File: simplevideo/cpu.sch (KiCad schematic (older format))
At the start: 8 parts, among them J2 Conn_01x08, J3 Conn_01x08, J4 Conn_01x08, J5 Conn_01x03, U18 WD65C02_, U19 74LS00, U27 28C256, U32 74LS138

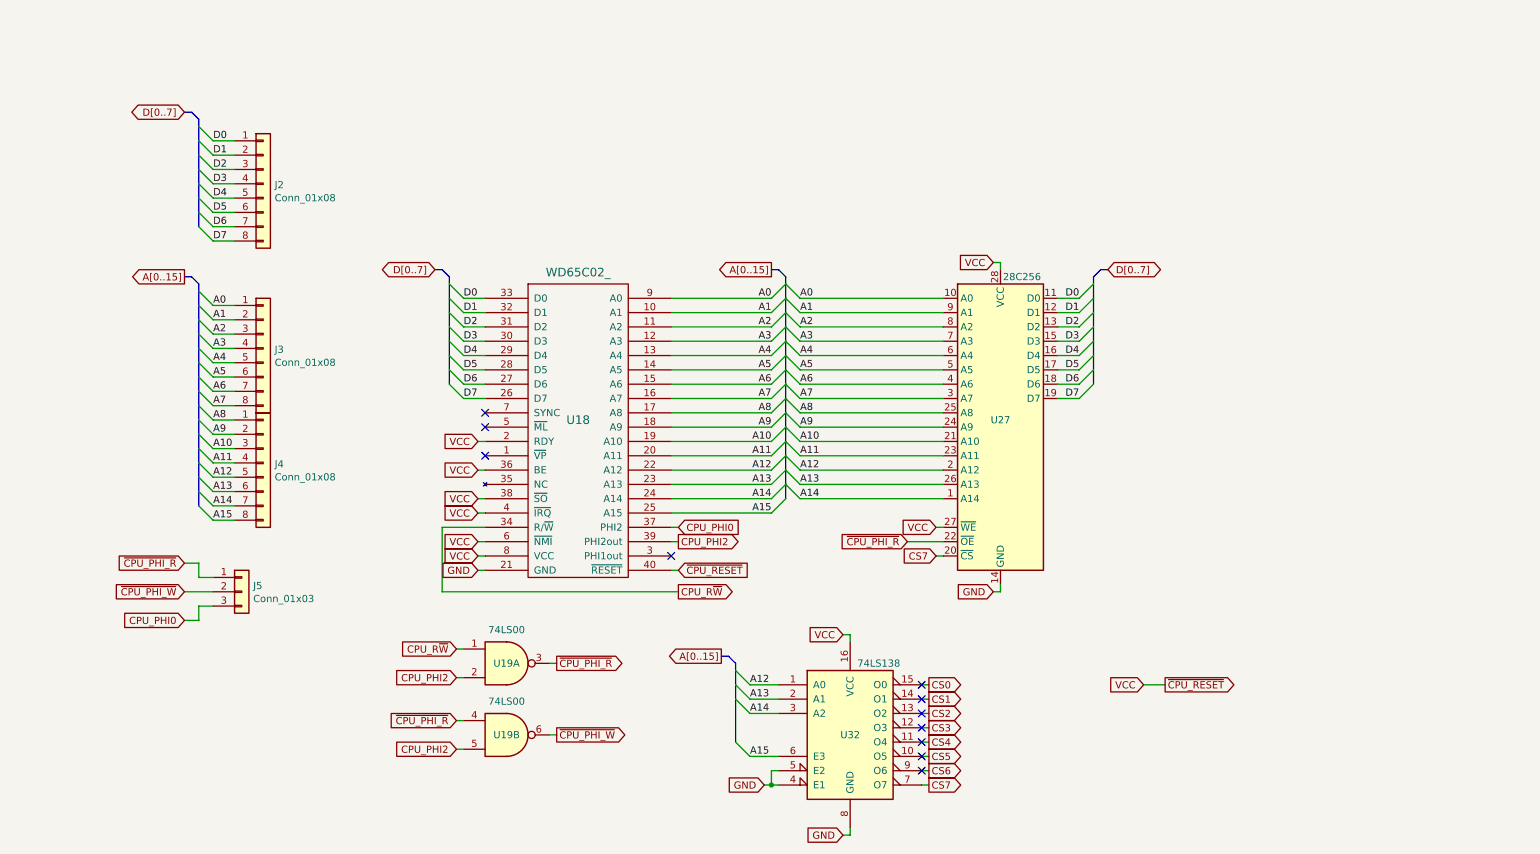
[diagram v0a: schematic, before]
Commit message: New address decoding scheme and complete breadboard layout, should be ready to build
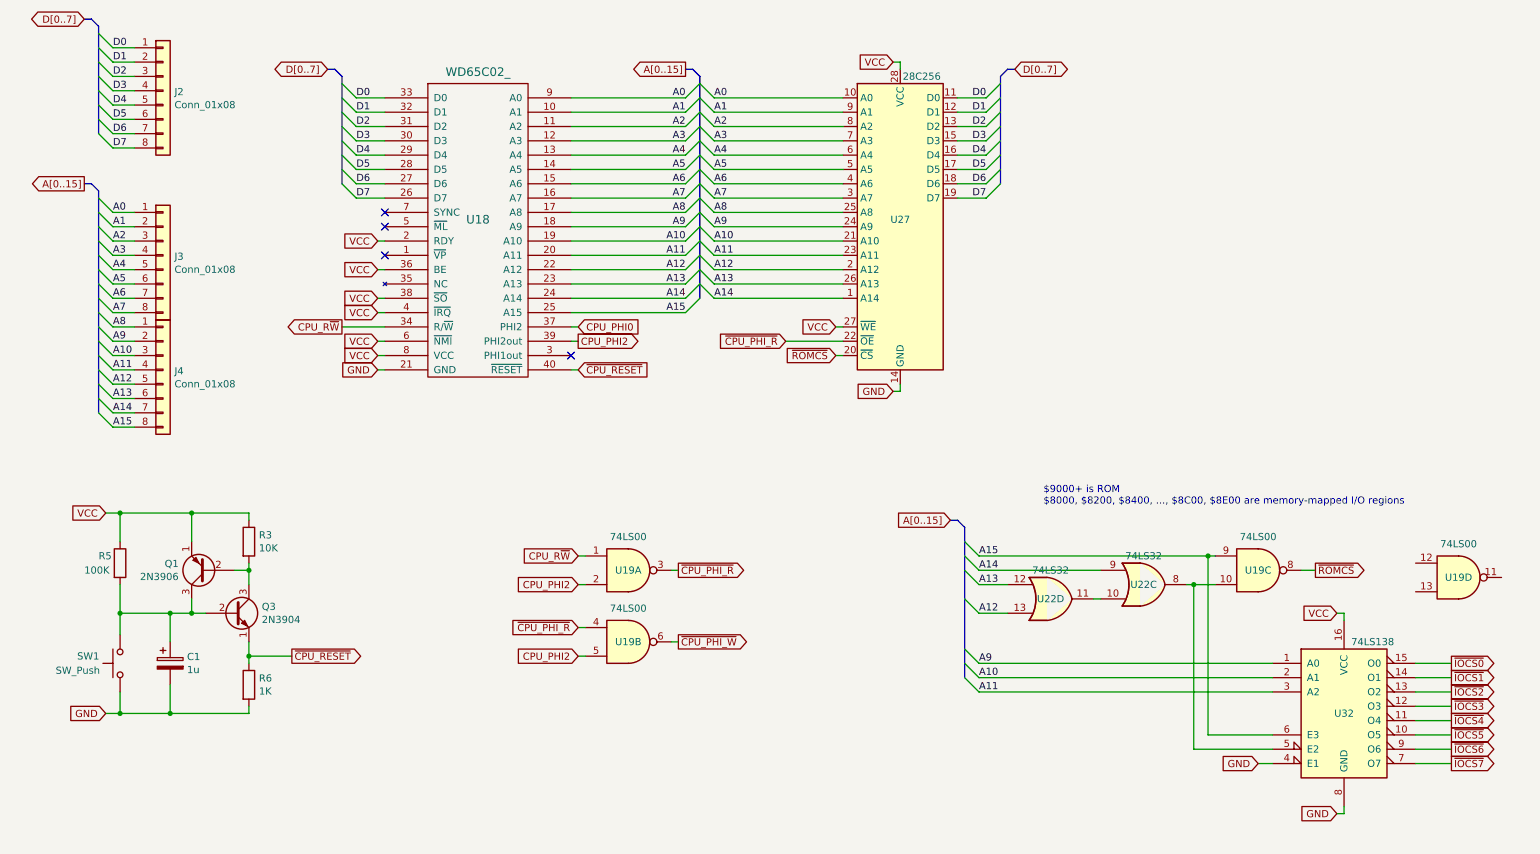
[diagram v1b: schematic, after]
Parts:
- removed J5: Conn_01x03, Connector_PinHeader_2.54mm:PinHeader_1x03_P2.54mm_Vertical, symbol Connector_Generic:Conn_01x03
- added C1: 1u, Capacitor_THT:CP_Radial_D5.0mm_P2.50mm, symbol Device:CP
- added Q1: 2N3906, Package_TO_SOT_THT:TO-92_Inline, symbol Transistor_BJT:2N3906
- added Q3: 2N3904, Package_TO_SOT_THT:TO-92_Inline, symbol Transistor_BJT:2N3904
- added R3: 10K, Resistor_THT:R_Axial_DIN0207_L6.3mm_D2.5mm_P7.62mm_Horizontal, symbol Device:R
- added R5: 100K, Resistor_THT:R_Axial_DIN0207_L6.3mm_D2.5mm_P7.62mm_Horizontal, symbol Device:R
- added R6: 1K, Resistor_THT:R_Axial_DIN0207_L6.3mm_D2.5mm_P7.62mm_Horizontal, symbol Device:R
- added SW1: SW_Push, Button_Switch_THT:SW_PUSH_6mm, symbol Switch:SW_Push
- added unit 3 of U19
- added unit 4 of U19
- added U22: 74LS32, Package_DIP:DIP-14_W7.62mm, symbol 74xx:74LS32
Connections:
- net A10: now also U32.2 (A1)
- net A11: now also U32.3 (A2)
- net A12: now also U22.13; no longer U32.1 (A0)
- net A13: now also U22.12; no longer U32.2 (A1)
- net A14: now also U22.9; no longer U32.3 (A2)
- net A15: now also U19.9
- net A9: now also U32.1 (A0)
- net GND: now also C1.2, R6.2, SW1.1; no longer U32.5 (E2)
- net VCC: now also Q1.1 (E), R3.1, R5.1; no longer U18.40 (~RESET)
- net CS0 renamed ~IOCS0
- net CS1 renamed ~IOCS1
- net CS2 renamed ~IOCS2
- net CS3 renamed ~IOCS3
- net CS4 renamed ~IOCS4
- net CS5 renamed ~IOCS5
- net CS6 renamed ~IOCS6
- net CS7 renamed ~IOCS7
- net ~IOCS7: no longer U27.20 (~CS)
- new net: U22.10, U22.11
- new net: C1.1, Q1.3 (C), Q3.2 (B), R5.2, SW1.2
- new net: Q1.2 (B), Q3.3 (C), R3.2
- new net: U19.10, U22.8, U32.5 (E2)
- new net ~CPU_RESET: Q3.1 (E), R6.1, U18.40 (~RESET)
- new net ~ROMCS: U19.8, U27.20 (~CS)
- no-connect marks 11 -> 4
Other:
- note added: "$9000+ is ROM\n$8000, $8200, $8400, ..., $8C00, $8E00 are memory-mapped I/O regions"
- moved on the sheet: J2, J3, J4, U18, U19A, U19B, U27

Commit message: Fixed various issues discovered during building and testing
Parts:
- removed unit 4 of U19
- added R11: 100K, Resistor_THT:R_Axial_DIN0207_L6.3mm_D2.5mm_P7.62mm_Horizontal, symbol Device:R
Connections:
- net CPU_PHI0: now also U19.2, U19.5
- net VCC: now also R11.2; no longer U18.2 (RDY)
- removed net CPU_PHI2: U18.39 (PHI2out), U19.2, U19.5
- new net: R11.1, U18.2 (RDY)
- no-connect marks 4 -> 5
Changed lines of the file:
@@
 Wire Wire Line
 	3150 2450 3200 2450
-Text GLabel 3150 2250 0    50   Input ~ 0
+Text GLabel 2700 2250 0    50   Input ~ 0
 VCC
-Wire Wire Line
-	3150 2250 3200 2250
 Text GLabel 4550 2850 2    50   Input ~ 0
 CPU_PHI0
@@
 Wire Wire Line
 	4500 3150 4550 3150
-Wire Wire Line
-	4500 2950 4550 2950
-Text GLabel 4550 2950 2    50   Output ~ 0
-CPU_PHI2
 Text GLabel 4550 3150 2    50   Input ~ 0
 ~CPU_RESET
@@
 CPU_R~W
 Text GLabel 4550 4650 0    50   Input ~ 0
-CPU_PHI2
+CPU_PHI0
 $Comp
 L 74xx:74LS00 U19
@@
 Text GLabel 5250 4550 2    50   Output ~ 0
 ~CPU_PHI_R
-Text GLabel 4550 5150 0    50   Input ~ 0
-CPU_PHI2
 $Comp
 L 74xx:74LS00 U19
@@
 $Comp
 L 74xx:74LS00 U19
-U 4 1 5F2C19C5
-P 10700 4600
-F 0 "U19" H 10700 4600 50  0000 C CNN
-F 1 "74LS00" H 10700 4834 50  0000 C CNN
-F 2 "Package_DIP:DIP-14_W7.62mm" H 10700 4600 50  0001 C CNN
-F 3 "http://www.ti.com/lit/gpn/sn74ls00" H 10700 4600 50  0001 C CNN
-	4    10700 4600
-	1    0    0    -1
-$EndComp
-$Comp
-L 74xx:74LS00 U19
 U 3 1 5F2C0E11
 P 9300 4550
@@
 Wire Bus Line
 	7250 4250 7200 4200
+$Comp
+L Device:R R11
+U 1 1 5EF3A894
+P 2950 2250
+F 0 "R11" V 2743 2250 50  0000 C CNN
+F 1 "100K" V 2834 2250 50  0000 C CNN
+F 2 "Resistor_THT:R_Axial_DIN0207_L6.3mm_D2.5mm_P7.62mm_Horizontal" V 2880 2250 50  0001 C CNN
+F 3 "~" H 2950 2250 50  0001 C CNN
+	1    2950 2250
+	0    1    1    0
+$EndComp
+Wire Wire Line
+	3100 2250 3200 2250
+Wire Wire Line
+	2800 2250 2700 2250
+NoConn ~ 4500 2950
 Wire Bus Line
 	7250 4250 7250 5300
@@
 Wire Bus Line
 	5400 1100 5400 2650
+Text GLabel 4550 5150 0    50   Input ~ 0
+CPU_PHI0
 $EndSCHEMATC
